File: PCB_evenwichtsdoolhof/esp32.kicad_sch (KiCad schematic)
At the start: 14 parts, among them J2 Conn_01x04_Pin, SW1 EN, SW2 FLASH, U1 ESP32-WROOM-32

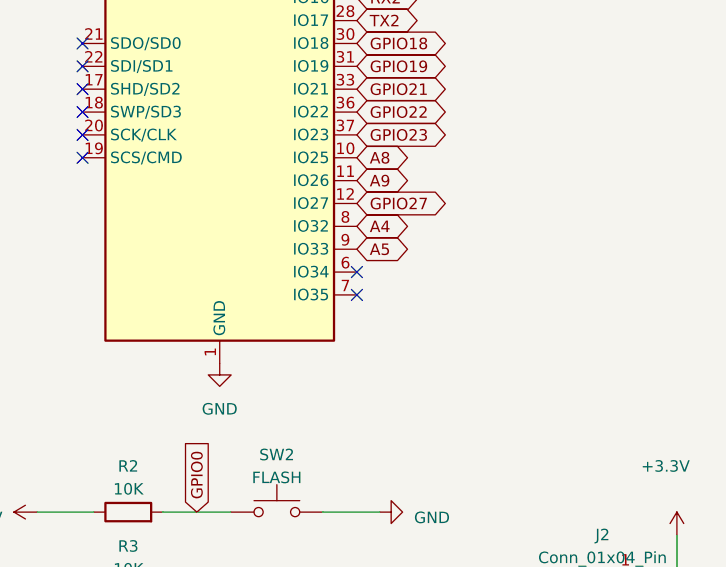
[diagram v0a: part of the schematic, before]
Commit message: File Restructuring
Restructuring and removing old files
+ cleaning up code
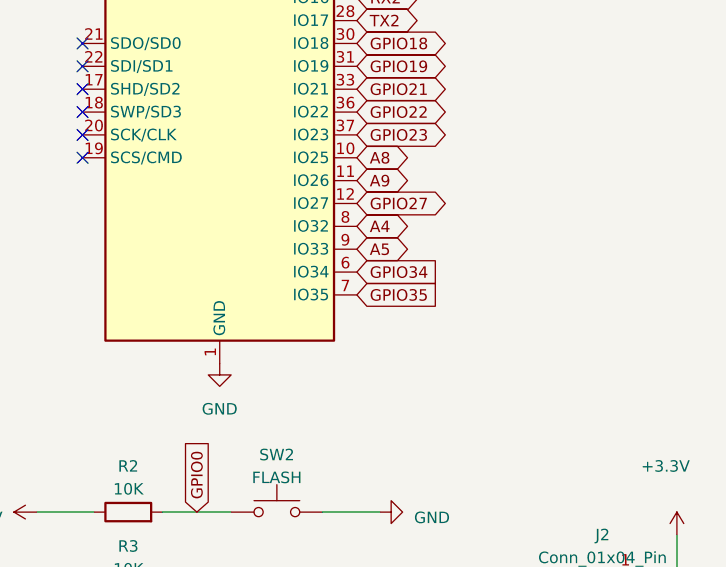
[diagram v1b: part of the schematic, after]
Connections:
- net GPIO34: now reaches U1.6 (IO34)
- net GPIO35: now reaches U1.7 (IO35)
- no-connect marks 10 -> 8
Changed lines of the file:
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@@
   (junction (at 60.96 30.48) (diameter 0) (color 0 0 0 0)
   )
-  (no_connect (at 78.74 97.79))
   (no_connect (at 48.26 46.99))
-  (no_connect (at 78.74 100.33))
   (no_connect (at 48.26 85.09))
   (no_connect (at 48.26 49.53))
@@
     )
   )
+  (global_label "GPIO34" (shape input) (at 78.74 97.79 0) (fields_autoplaced)
+    (effects (font (size 1.27 1.27)) (justify left))
+    (property "Intersheetrefs" "${INTERSHEET_REFS}" (at 88.5401 97.79 0)
+      (effects (font (size 1.27 1.27)) (justify left) hide)
+    )
+  )
   (global_label "A9" (shape bidirectional) (at 78.74 87.63 0) (fields_autoplaced)
     (effects (font (size 1.27 1.27)) (justify left))
@@
       (effects (font (size 1.27 1.27)) (justify left) hide)
     )
+  )
+  (global_label "GPIO35" (shape input) (at 78.74 100.33 0) (fields_autoplaced)
+    (effects (font (size 1.27 1.27)) (justify left))
+    (property "Intersheetrefs" "${INTERSHEET_REFS}" (at 88.5401 100.33 0)
+      (effects (font (size 1.27 1.27)) (justify left) hide)
+    )
